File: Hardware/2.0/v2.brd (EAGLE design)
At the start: 75.9 x 67.3 mm, 63 parts, among them IC1 LM386N-1, IC3 PCF8563, IC5 7805TV, IC9 TL074P, K1 SRD-5VDC-SL-C, K2 SRD-5VDC-SL-C, K3 SRD-5VDC-SL-C, K4 SRD-5VDC-SL-C, Q4 32768 hz, T1 BC639, T2 BC639, T3 BC639, T4 BC639

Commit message: poczatki pracy nad v2.0
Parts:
- removed C11, C14: 100n, rcl:C1206
- removed C13: 220n, rcl:C050-025X075
- removed D1, D2, D3, D4: 1N4148, diode:DO41-10
- removed IC2: (no value), ads11xx:SOT-23-6
- removed IC9: TL074P, linear:DIL14
- removed JP2: Wej audio, pinhead:1X02
- removed JP5: BATERY_OFF, jumper:JP1
- removed JP6: Elektroda_Ph, pinhead:1X02
- removed K1, K2, K3, K4: SRD-5VDC-SL-C, relay:ZF112
- removed R1, R2, R3, R4: 470, rcl:0204/7
- removed R11, R12: 4,7k, my_library:0207/10
- removed R16: 470, my_library:0207/10
- removed R25: 0R, rcl:R1206
- removed R26: 50k, rcl:RTRIM64X
- removed R30, R31: 220k, rcl:R1206
- removed R32, R36: 10k, rcl:R1206
- removed R33, R34: 4k7, rcl:R1206
- removed R35: 1k, rcl:RTRIM64X
- removed T1, T2, T3, T4: BC639, transistor:TO92-ECB
- removed X1, X2, X3, X4: (no value), con-wago-500:W237-103
- added AU_IN: Wej audio, pinhead:1X02
- added AU_OUT: Glosnik, pinhead:1X02
- added IC4: ULN2803A, uln-udn:DIL18
- added R10: 470, rcl:R1206
- added R8, R9: 4,7k, rcl:R1206
- added X5: (no value), con-subd:M09H
- JP3: value Glosnik -> (none); device pinhead:1X02 -> pinhead:1X05/90
- R5: device rcl:0207/7 -> rcl:R1206
- R6: device rcl:0204/7 -> rcl:R1206
- moved C6 325.0 mm to (72.4, 48.3)
- moved D5 324.3 mm to (66.0, 43.2), turned to 90 degrees
- moved BAT1 321.9 mm to (72.4, 62.2), turned to 90 degrees
- moved D6 317.3 mm to (61.0, 40.6), turned to 180 degrees
- moved IC3 303.9 mm to (61.0, 33.0), turned to 270 degrees
- moved Q4 299.5 mm to (53.3, 35.6), turned to 90 degrees
- moved C7 296.1 mm to (45.7, 35.6)
- moved C17 256.4 mm to (24.1, 40.6)
- moved C18 255.6 mm to (24.1, 31.8), turned to 180 degrees
- moved C16 254.1 mm to (24.1, 36.8), turned to 180 degrees
- moved VCC_LED 248.2 mm to (0.00, 27.9), turned to 270 degrees
- moved 12V_INPUT 237.1 mm to (7.62, 36.8), turned to 270 degrees
- moved IC5 229.4 mm to (19.1, 35.6), turned to 270 degrees
- moved JP3 163.4 mm to (76.2, 31.8), turned to 180 degrees
- moved JP4 151.4 mm to (3.81, 45.7), turned to 270 degrees
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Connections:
- removed net N$100: C11.2, R30.2, R31.1
- removed net N$102: C14.1, IC9.5, R31.2
- removed net N$104: C11.1, IC9.6, IC9.7, R25.2
- removed net N$109: IC9.9, R33.2, R34.2
- removed net N$110: IC9.8, R32.2, R33.1
- removed net N$12: R2.1, T2.B
- removed net N$13: D3.A, K2.2, T3.C
- removed net N$14: K1.P, X3.2
- removed net N$15: K1.S, X3.3
- removed net N$16: K1.O, X3.1
- removed net N$17: R3.1, T3.B
- removed net N$19: K2.P, X2.2
- removed net N$20: K2.S, X2.3
- removed net N$21: K2.O, X2.1
- removed net N$23: JP1.18, R3.2
- removed net N$25: D4.A, K4.2, T4.C
- removed net N$26: R4.1, T4.B
- removed net N$28: K4.P, X4.2
- removed net N$29: K4.S, X4.3
- removed net N$31: K4.O, X4.1
- removed net N$32: JP1.22, R4.2
- removed net N$46: C13.1, IC9.3, JP6.2
- removed net N$47: IC9.12, R35.2, R35.3, R36.2
- removed net N$5: R1.1, T1.B
- removed net N$51: IC9.10, R25.1
- removed net N$94: IC9.13, R26.1, R32.1
- removed net N$96: IC9.1, IC9.2, R30.1
- removed net PHOUT: IC2.1, IC9.14, R26.2, R26.3
- removed net V+: IC9.4
- removed net V-: IC9.11
- new net N$37: IC4.18, X5.5
- new net N$39: IC4.16, X5.4
- new net N$40: IC4.15, X5.8
- new net N$41: IC4.14, X5.3
- new net N$42: IC4.13, X5.7
- new net N$49: IC4.2, JP1.11
- net +12V: now also IC4.10, JP3.1, X5.6
- net +5V: now also JP3.2, R8.2, R9.2; no longer D1.C, D2.C, D3.C, D4.C, IC2.5, K1.1, K2.1, K3.1, K4.1, R11.1, R12.1, R36.1
- net GND: now also AU_IN.1, AU_OUT.1, IC4.9, JP3.3, R10.1, X5.1; no longer C13.2, C14.2, IC2.2, IC2.6, JP2.1, JP3.1, JP6.1, R16.2, R34.1, R35.1, T1.E, T2.E, T3.E, T4.E
- net N$1: now also IC4.3, JP1.13; no longer JP1.12, R1.2
- net N$10: now also IC4.6, JP1.18; no longer D2.A, K1.2, T2.C
- net N$2: now also IC4.4, JP1.16; no longer D1.A, K3.2, T1.C
- net N$22: now also IC4.17, X5.9; no longer C6.+, D6.C, IC3.8, JP5.2
- net N$24: now also C6.+, D6.C, IC3.8; no longer JP5.1
- net N$3: now also IC4.1, JP1.12; no longer JP1.16, R2.2
- net N$33: now also R10.2; no longer R16.1
- net N$6: now also IC4.12, X5.2; no longer K3.P, X1.2
- net N$61: now also AU_OUT.2; no longer JP3.2
- net N$64: now also AU_IN.2; no longer JP2.2
- net N$7: now also IC4.7, JP1.22; no longer K3.S, X1.3
- net N$8: now also IC4.5, JP1.15; no longer K3.O, X1.1
- net SCL: now also JP3.4, R9.1; no longer IC2.3, R12.2
- net SDA: now also JP3.5, R8.1; no longer IC2.4, R11.2
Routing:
- net GND: track 100.3 -> 347.2 mm, vias 2 -> 0
- net +12V: track 0.00 -> 199.3 mm, vias 0 -> 2
- net N$11: track 0.00 -> 96.5 mm
- net N$18: track 8.89 -> 93.2 mm
- net SDA: track 0.00 -> 67.6 mm
- net SCL: track 0.00 -> 64.6 mm
- net N$49: track 0.00 -> 53.8 mm, vias 1 -> 0
- net N$32: track 44.4 -> 0.00 mm
- net N$60: track 0.00 -> 43.7 mm
- net N$23: track 41.9 -> 0.00 mm
- net N$8: track 10.8 -> 44.1 mm
- net N$2: track 17.1 -> 50.2 mm
- net N$7: track 10.8 -> 36.2 mm
- net N$28: track 24.7 -> 0.00 mm
- net N$19: track 24.7 -> 0.00 mm
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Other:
- board size 75.9 x 67.3 mm -> 86 x 58.4 mm
- board text added: "AquaPI Core v2.0"
- board text removed: "AquaPI"
- board text removed: "v 0.1"

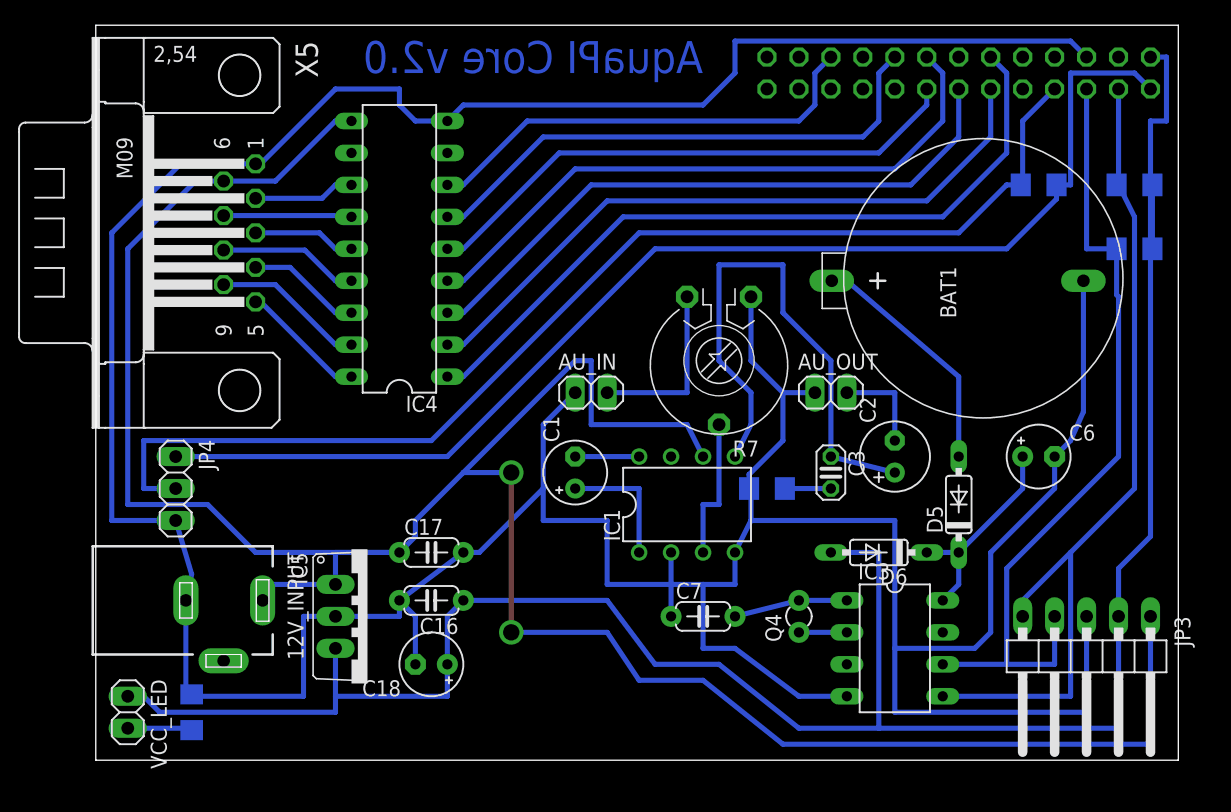
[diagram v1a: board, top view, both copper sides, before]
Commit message: - uproszczenie & wersja gotowa do testów
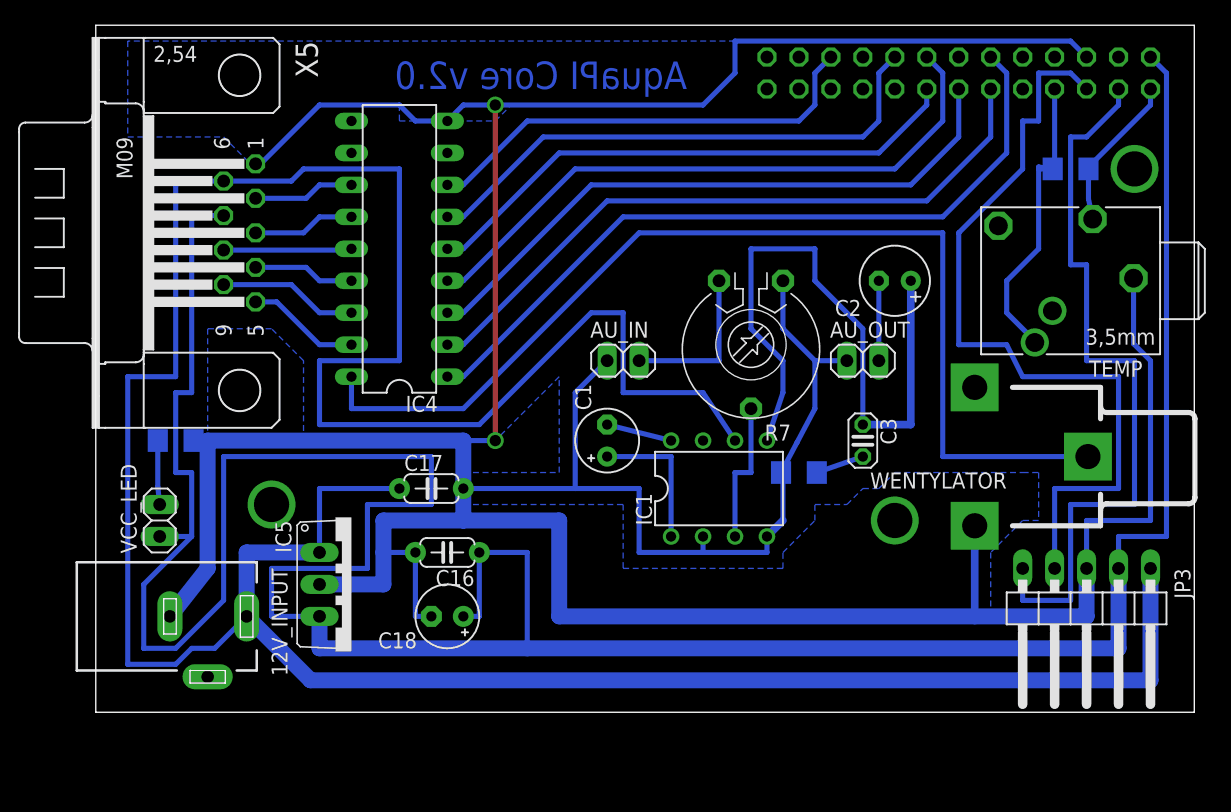
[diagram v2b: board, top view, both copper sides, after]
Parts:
- removed BAT1: CR2032, sn2032:SN2932_LISPOL
- removed C6: 22uF, my_library:E2,5-5
- removed C7: 33 pF, my_library:C050-024X044
- removed D5, D6: 1N4148, my_library:DO35-7
- removed IC3: PCF8563, my_library:DIL08
- removed JP4: 1-wire temp, pinhead:1X03
- removed Q4: 32768 hz, my_library:TC26V
- removed R8, R9: 4,7k, rcl:R1206
- added TEMP: PG203J, con-hirschmann:PG203J
- added WENTYLATOR: 736880-49, con-conrad:736880-49
- moved R10 21.6 mm to (3.81, 49.5), turned to 0 degrees
- moved VCC_LED 15.5 mm to (2.54, 43.2), turned to 90 degrees
- moved C2 14.0 mm to (61.0, 62.2), turned to 180 degrees
- moved C17 5.08 mm to (24.1, 45.7)
- moved C16 4.02 mm to (25.4, 40.6)
- moved C18 4.02 mm to (25.4, 35.6)
- moved JP3 3.81 mm to (76.2, 35.6)
- moved AU_IN 3.59 mm to (39.4, 55.9)
- moved AU_OUT 3.59 mm to (58.4, 55.9)
- moved C1 3.59 mm to (38.1, 49.5)
- moved C3 3.59 mm to (58.4, 49.5)
- moved R5 2.84 mm to (74.9, 71.1)
- moved R6 2.84 mm to (53.3, 47.0)
- moved IC5 2.84 mm to (17.8, 38.1)
- moved IC1 2.84 mm to (47.0, 45.7)
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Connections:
- removed net N$24: C6.+, D5.C, D6.C, IC3.8
- removed net N$27: BAT1.+, D5.A
- removed net N$39: IC4.16, X5.4
- removed net N$41: IC4.14, X5.3
- removed net N$42: IC4.13, X5.7
- new net N$5: IC4.16, X5.9
- net +12V: no longer IC4.10
- net +5V: now also X5.7; no longer D6.A, R8.2, R9.2
- net GND: now also TEMP.1, WENTYLATOR.2; no longer BAT1.-, C6.-, C7.1, IC3.4, JP4.3
- net N$11: now also TEMP.5; no longer JP4.1
- net N$18: now also TEMP.2; no longer JP4.2
- net N$22: now also X5.5; no longer X5.9
- net N$37: now also WENTYLATOR.1; no longer X5.5
- net N$4: now also IC4.13, X5.3; no longer IC3.2, Q4.1
- net N$40: now also X5.4; no longer X5.8
- net N$9: now also IC4.14, X5.8; no longer C7.2, IC3.1, Q4.2
- net SCL: no longer IC3.6, R9.1
- net SDA: no longer IC3.5, R8.1
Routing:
- net N$11: track 96.5 -> 12.6 mm
- net N$37: track 10.1 -> 84.6 mm
- net N$18: track 93.2 -> 24.7 mm
- net +5V: track 175.5 -> 243.8 mm
- net +12V: track 199.3 -> 248.1 mm, vias 2 -> 0
- net N$27: track 19.3 -> 0.00 mm
- net N$24: track 16.6 -> 0.00 mm
- net GND: track 347.2 -> 335.5 mm, vias 0 -> 2
- net N$5: track 0.00 -> 11.1 mm
- net N$42: track 10.2 -> 0.00 mm
- net N$39: track 9.11 -> 0.00 mm
- net N$60: track 43.7 -> 52.4 mm
- net SDA: track 67.6 -> 59.5 mm
- net N$41: track 8.15 -> 0.00 mm
- net N$4: track 3.81 -> 8.15 mm
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- added copper zone on layer 16, net GND
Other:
- board size 86 x 58.4 mm -> 87.3 x 54.6 mm
